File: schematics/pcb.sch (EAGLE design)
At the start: 39 parts, among them IC1 7805TV, IC2 4050D, IC3 LP298XS, Q1 16Mhz, Q2 16Mhz, X1 MICROSD

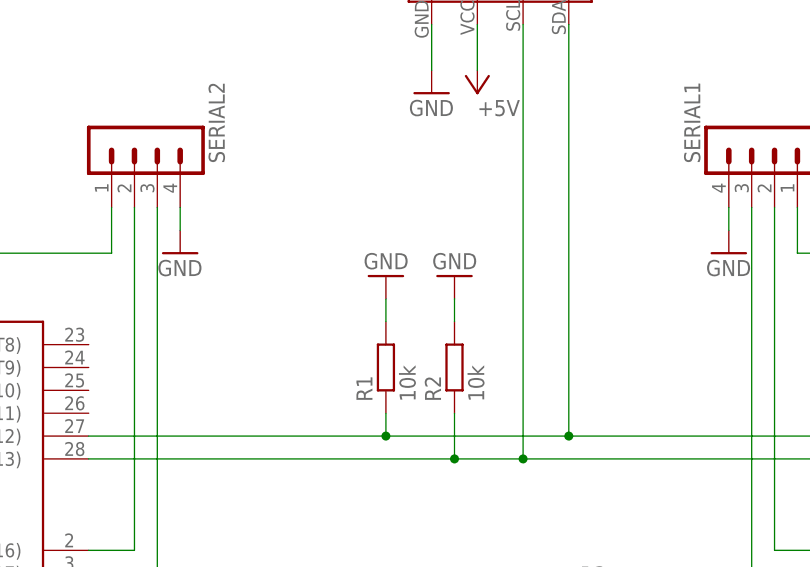
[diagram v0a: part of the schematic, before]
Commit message: Fixed I2C Pull-ups being Pull-downs
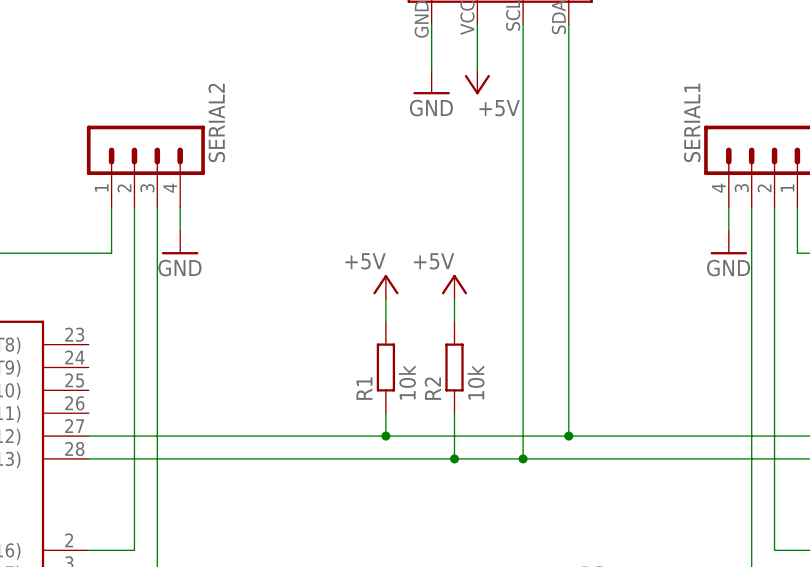
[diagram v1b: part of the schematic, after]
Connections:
- net +5V: now also R1.2, R2.2
- net GND: no longer R1.2, R2.2
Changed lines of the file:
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@@
 <part name="GND1" library="supply1" library_urn="urn:adsk.eagle:library:371" deviceset="GND" device=""/>
 <part name="GND3" library="supply1" library_urn="urn:adsk.eagle:library:371" deviceset="GND" device=""/>
-<part name="GND4" library="supply1" library_urn="urn:adsk.eagle:library:371" deviceset="GND" device=""/>
-<part name="GND5" library="supply1" library_urn="urn:adsk.eagle:library:371" deviceset="GND" device=""/>
 <part name="R1" library="rcl" library_urn="urn:adsk.eagle:library:334" deviceset="R-EU_" device="R0805" package3d_urn="urn:adsk.eagle:package:23553/2" value="10k"/>
 <part name="R2" library="rcl" library_urn="urn:adsk.eagle:library:334" deviceset="R-EU_" device="R0805" package3d_urn="urn:adsk.eagle:package:23553/2" value="10k"/>
@@
 <part name="GND23" library="supply1" library_urn="urn:adsk.eagle:library:371" deviceset="GND" device=""/>
 <part name="GND24" library="supply1" library_urn="urn:adsk.eagle:library:371" deviceset="GND" device=""/>
+<part name="P+1" library="supply1" library_urn="urn:adsk.eagle:library:371" deviceset="+5V" device=""/>
+<part name="P+13" library="supply1" library_urn="urn:adsk.eagle:library:371" deviceset="+5V" device=""/>
 </parts>
 <sheets>
@@
 <attribute name="VALUE" x="248.92" y="30.48" size="1.778" layer="96" rot="MR270"/>
 </instance>
-<instance part="GND4" gate="1" x="127" y="91.44" smashed="yes" rot="R180">
-<attribute name="VALUE" x="129.54" y="93.98" size="1.778" layer="96" rot="R180"/>
-</instance>
-<instance part="GND5" gate="1" x="119.38" y="91.44" smashed="yes" rot="R180">
-<attribute name="VALUE" x="121.92" y="93.98" size="1.778" layer="96" rot="R180"/>
-</instance>
 <instance part="R1" gate="G$1" x="119.38" y="81.28" smashed="yes" rot="R90">
 <attribute name="NAME" x="117.8814" y="77.47" size="1.778" layer="95" rot="R90"/>
@@
 <instance part="GND24" gate="1" x="157.48" y="93.98" smashed="yes">
 <attribute name="VALUE" x="154.94" y="91.44" size="1.778" layer="96"/>
+</instance>
+<instance part="P+1" gate="1" x="119.38" y="91.44" smashed="yes">
+<attribute name="VALUE" x="119.38" y="93.98" size="1.778" layer="96" rot="R180"/>
+</instance>
+<instance part="P+13" gate="1" x="127" y="91.44" smashed="yes">
+<attribute name="VALUE" x="127" y="93.98" size="1.778" layer="96" rot="R180"/>
 </instance>
 </instances>
@@
 </segment>
 <segment>
-<pinref part="GND5" gate="1" pin="GND"/>
-<pinref part="R1" gate="G$1" pin="2"/>
-<wire x1="119.38" y1="88.9" x2="119.38" y2="86.36" width="0.1524" layer="91"/>
-</segment>
-<segment>
-<pinref part="R2" gate="G$1" pin="2"/>
-<pinref part="GND4" gate="1" pin="GND"/>
-<wire x1="127" y1="86.36" x2="127" y2="88.9" width="0.1524" layer="91"/>
-</segment>
-<segment>
 <pinref part="C1" gate="G$1" pin="1"/>
 <wire x1="0" y1="71.12" x2="-2.54" y2="71.12" width="0.1524" layer="91"/>
@@
 <wire x1="81.28" y1="-22.86" x2="81.28" y2="-27.94" width="0.1524" layer="91"/>
 </segment>
+<segment>
+<pinref part="P+1" gate="1" pin="+5V"/>
+<pinref part="R1" gate="G$1" pin="2"/>
+<wire x1="119.38" y1="88.9" x2="119.38" y2="86.36" width="0.1524" layer="91"/>
+</segment>
+<segment>
+<pinref part="R2" gate="G$1" pin="2"/>
+<pinref part="P+13" gate="1" pin="+5V"/>
+<wire x1="127" y1="88.9" x2="127" y2="86.36" width="0.1524" layer="91"/>
+</segment>
 </net>
